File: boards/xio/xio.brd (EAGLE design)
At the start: 170 x 170 mm, 122 parts, among them IC1 AS4C16M16SA-C, IC2 74LVC1G02DBV, IC3 IDTQS3245QSOP20, IC4 IDTQS3245QSOP20, IC5 IDTQS3245QSOP20, IC6 IDTQS3245QSOP20, IC7 IDTQS3245QSOP20, U1 24 MHz Osc. (F535L-24), X1 PCI-E-164SOCKET, X2 PCI-E-164SOCKET, X3 PCI-E-164SOCKET, X4 PCI-E-164SOCKET, X5 PCI-E-164SOCKET, X6 PCI-E-164SOCKET, X7 PCI-E-164SOCKET

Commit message: Start on STM32 power
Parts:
- added C57: 10uF, rcl:C0402K
- added C58: 0.1uF, rcl:C0402K
- added C59, C60: 2.2uF, rcl:C0402K
- added SWD: FTSH-105-01-LM-DV-K, sjg-stm32:SWD_DEBUG
- U$3: value LD49150 -> LD49300
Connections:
- removed net N$4: C31.2, R3.1, U$3.1, U$4.6
- removed net VCCIO: C31.1, R3.2
- new net DBG_RX: SWD.P8, U$22.B4
- new net DBG_TX: SWD.P6, U$22.A7
- new net EN_1V0: R3.1, U$3.1, U$4.1
- new net SWD_CLK: SWD.P4, U$22.A14
- new net SWD_IO: SWD.P2, U$22.A13
- new net VCAP1: C59.1, U$22.L11
- new net VCAP2: C60.1, U$22.E11
- net !RESET!: now also SWD.P10, U$22.J1
- net +3V3: now also C31.1, C57.1, C58.1, R3.2, SWD.P1, U$22.C1, U$22.E10, U$22.E5, U$22.E7, U$22.E8, U$22.E9, U$22.F11, U$22.F4, U$22.F5, U$22.G5, U$22.H11, U$22.H5, U$22.J11, U$22.J5, U$22.K11, U$22.K5, U$22.L10, U$22.L7, U$22.L8, U$22.L9, U$22.P1, U$22.R1, U$4.6
- net GND: now also C31.2, C57.2, C58.2, C59.2, C60.2, SWD.P3, SWD.P5, SWD.P9, U$22.E6, U$22.F10, U$22.F2, U$22.F6, U$22.F7, U$22.F8, U$22.F9, U$22.G10, U$22.G6, U$22.H10, U$22.H6, U$22.J10, U$22.J6, U$22.K10, U$22.K6, U$22.K7, U$22.K8, U$22.K9, U$22.L5, U$22.L6, U$22.M1, U$22.N1

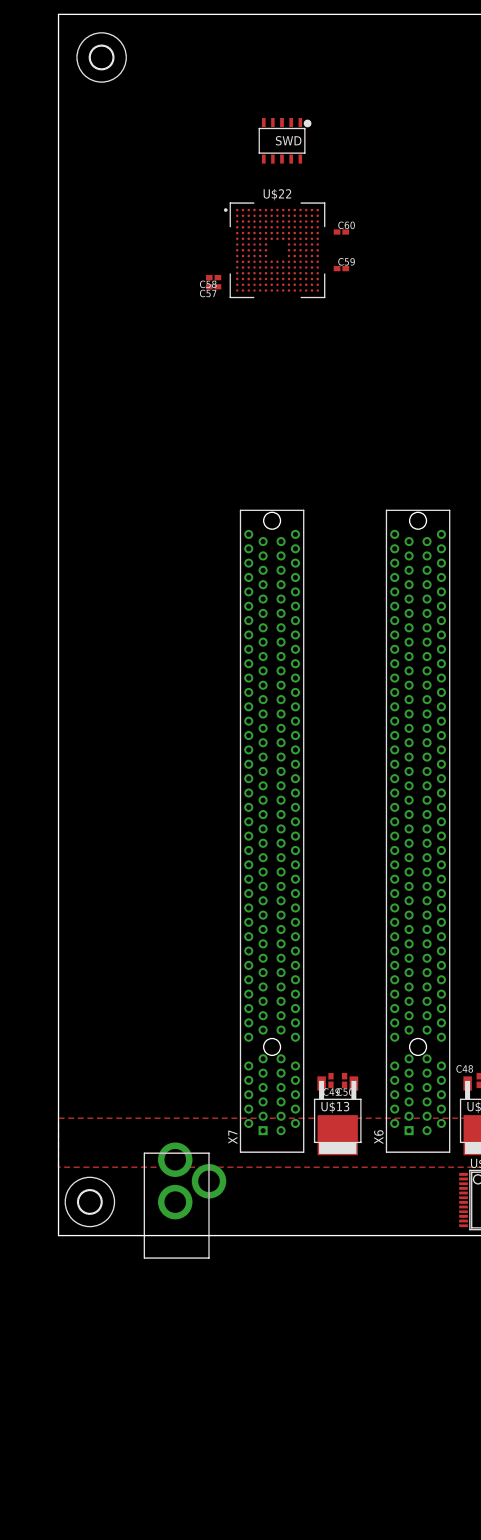
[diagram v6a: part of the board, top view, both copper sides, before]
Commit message: - Implement I2C - Implement SPI - Implement debug leds - Start to implement dual UARTs
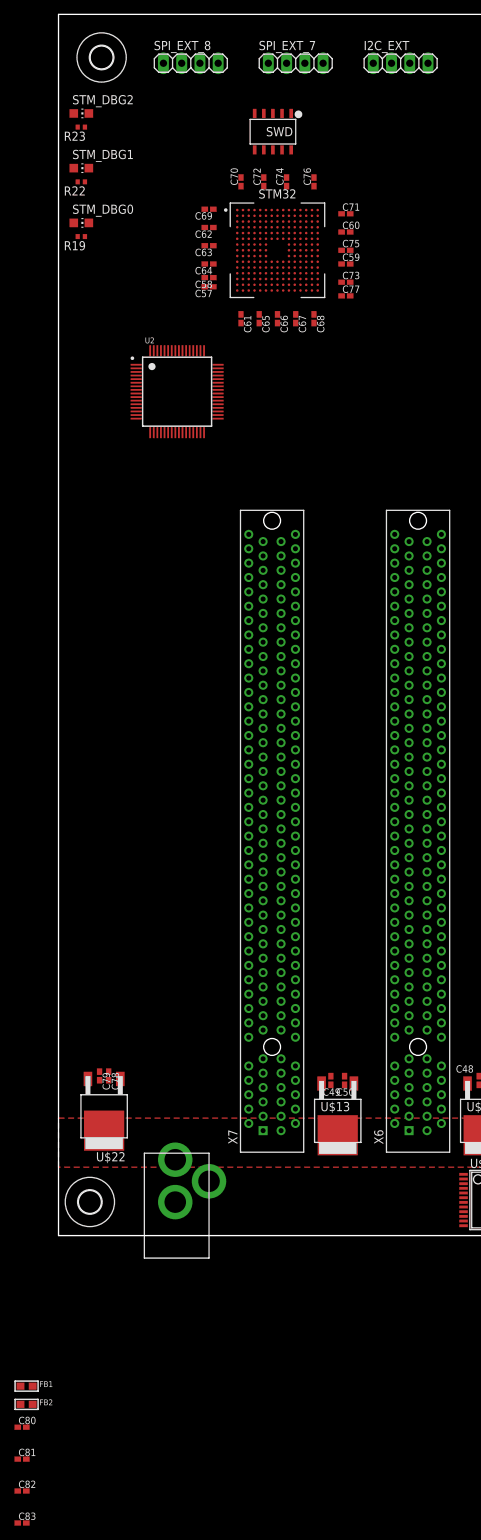
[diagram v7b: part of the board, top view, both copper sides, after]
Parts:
- added C61, C78, C79: 10uF, rcl:C0402K
- added C62, C63, C64, C65, C66, C67, C68, C69, C70, C71, C72, C73, C74, C75, C76, C77, C82, C83: 0.1uF, rcl:C0402K
- added C80, C81: 4.7uF, rcl:C0402K
- added FB1, FB2: 742792651, microbuilder:0603
- added I2C_EXT, SPI_EXT_7, SPI_EXT_8: (no value), pinhead:1X04
- added R19, R22, R23: 1K, rcl:R0402
- added STM32: STM32F777N, sjg-stm32:BGA216C80P15X15_1300X1300X110
- added STM_DBG0, STM_DBG1, STM_DBG2: ok33, led:CHIP-LED0805
- added U2: (no value), microbuilder:LQFP64
- U$22: value STM32F777N -> AP7363-18D-13; device sjg-stm32:BGA216C80P15X15_1300X1300X110 -> sjg-power:TO252-3L
- moved U$22 124.9 mm to (6.35, 14.6), turned to 180 degrees
- moved SWD 1.80 mm to (29.8, 153.7)
- moved C59 0.90 mm to (40.0, 135.3)
- moved C60 0.64 mm to (40.0, 139.7)
- moved C57 0.64 mm to (21.0, 132.1)
- moved C58 0.64 mm to (21.0, 133.3)
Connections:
- new net 1.8V: C79.1, U$22.P$3, U2.12, U2.37, U2.64
- new net I2C_SCL: I2C_EXT.1, I2C_EXT.3, STM32.R13, X1.B44, X2.B44, X3.B44, X4.B44, X5.B44, X6.B44, X7.B44
- new net I2C_SDA: I2C_EXT.2, I2C_EXT.4, STM32.P12, X1.B43, X2.B43, X3.B43, X4.B43, X5.B43, X6.B43, X7.B43
- new net N$17: STM32.K2, STM_DBG0.A
- new net N$20: STM32.K1, STM_DBG1.A
- new net N$21: STM32.A11, STM_DBG2.A
- new net N$22: C81.2, C82.2, FB1.1, U2.4
- new net N$25: R23.1, STM_DBG2.C
- new net N$26: R22.1, STM_DBG1.C
- new net N$27: R19.1, STM_DBG0.C
- new net N$4: C80.1, C83.1, FB2.2, U2.9
- new net PIO_IN0: STM32.R5, X1.B12, X2.B12, X3.B12, X4.B12, X5.B12, X6.B12, X7.B12
- new net PIO_IN1: STM32.R4, X1.B13, X2.B13, X3.B13, X4.B13, X5.B13, X6.B13, X7.B13
- new net PIO_IN2: STM32.M5, X1.B14, X2.B14, X3.B14, X4.B14, X5.B14, X6.B14, X7.B14
- new net PIO_IN3: STM32.A10, X1.B15, X2.B15, X3.B15, X4.B15, X5.B15, X6.B15, X7.B15
- new net PIO_IN4: STM32.A9, X1.B16, X2.B16, X3.B16, X4.B16, X5.B16, X6.B16, X7.B16
- new net PIO_IN5: STM32.A8, X1.B17, X2.B17, X3.B17, X4.B17, X5.B17, X6.B17, X7.B17
- new net PIO_IN6: STM32.B6, X1.B18, X2.B18, X3.B18, X4.B18, X5.B18, X6.B18, X7.B18
- new net PIO_IN7: STM32.B5, X1.B19, X2.B19, X3.B19, X4.B19, X5.B19, X6.B19, X7.B19
- new net PIO_IN_CLK: STM32.M3, X1.B20, X2.B20, X3.B20, X4.B20, X5.B20, X6.B20, X7.B20
- new net PIO_IN_RCV: STM32.H1, X1.B21, X2.B21, X3.B21, X4.B21, X5.B21, X6.B21, X7.B21
- new net PIO_IRQ0: STM32.R2, X1.B22, X2.B22, X3.B22, X4.B22, X5.B22, X6.B22, X7.B22
- new net PIO_IRQ1: STM32.N4, X1.B23, X2.B23, X3.B23, X4.B23, X5.B23, X6.B23, X7.B23
- new net PIO_IRQ2: STM32.P4, X1.B24, X2.B24, X3.B24, X4.B24, X5.B24, X6.B24, X7.B24
- new net PIO_IRQ3: STM32.P3, X1.B25, X2.B25, X3.B25, X4.B25, X5.B25, X6.B25, X7.B25
- new net PIO_IRQ4: STM32.A2, X1.B26, X2.B26, X3.B26, X4.B26, X5.B26, X6.B26, X7.B26
- new net PIO_IRQ5: STM32.A1, X1.B27, X2.B27, X3.B27, X4.B27, X5.B27, X6.B27, X7.B27
- new net PIO_IRQ6: STM32.B1, X1.B28, X2.B28, X3.B28, X4.B28, X5.B28, X6.B28, X7.B28
- new net PIO_IRQ7: STM32.B2, X1.B29, X2.B29, X3.B29, X4.B29, X5.B29, X6.B29, X7.B29
- new net PIO_OUT0: STM32.E14, X1.B30, X2.B30, X3.B30, X4.B30, X5.B30, X6.B30, X7.B30
- new net PIO_OUT1: STM32.D14, X1.B31, X2.B31, X3.B31, X4.B31, X5.B31, X6.B31, X7.B31
- new net PIO_OUT2: STM32.C14, X1.B32, X2.B32, X3.B32, X4.B32, X5.B32, X6.B32, X7.B32
- new net PIO_OUT3: STM32.C13, X1.B33, X2.B33, X3.B33, X4.B33, X5.B33, X6.B33, X7.B33
- new net PIO_OUT4: STM32.C3, X1.B34, X2.B34, X3.B34, X4.B34, X5.B34, X6.B34, X7.B34
- new net PIO_OUT5: STM32.D3, X1.B35, X2.B35, X3.B35, X4.B35, X5.B35, X6.B35, X7.B35
- new net PIO_OUT6: STM32.D6, X1.B36, X2.B36, X3.B36, X4.B36, X5.B36, X6.B36, X7.B36
- new net PIO_OUT7: STM32.D4, X1.B37, X2.B37, X3.B37, X4.B37, X5.B37, X6.B37, X7.B37
- new net PIO_OUT_CLK: STM32.M12, X1.B38, X2.B38, X3.B38, X4.B38, X5.B38, X6.B38, X7.B38
- new net PIO_OUT_RCV: STM32.H4, X1.B39, X2.B39, X3.B39, X4.B39, X5.B39, X6.B39, X7.B39
- new net PIO_SEL0: STM32.N10, X1.B40, X2.B40, X3.B40, X4.B40, X5.B40, X6.B40, X7.B40
- new net PIO_SEL1: STM32.M10, X1.B41, X2.B41, X3.B41, X4.B41, X5.B41, X6.B41, X7.B41
- new net PIO_SEL2: STM32.M11, X1.B42, X2.B42, X3.B42, X4.B42, X5.B42, X6.B42, X7.B42
- new net SPI_CLK: SPI_EXT_7.1, SPI_EXT_8.1, STM32.K14, X1.B45, X2.B45, X3.B45, X4.B45, X5.B45, X6.B45, X7.B45
- new net SPI_MISO: SPI_EXT_7.2, SPI_EXT_8.2, STM32.R14, X1.B46, X2.B46, X3.B46, X4.B46, X5.B46, X6.B46, X7.B46
- new net SPI_MOSI: SPI_EXT_7.3, SPI_EXT_8.3, STM32.R15, X1.B47, X2.B47, X3.B47, X4.B47, X5.B47, X6.B47, X7.B47
- new net SPI_SS0: STM32.J15, X1.B48
- new net SPI_SS1: STM32.J14, X2.B48
- new net SPI_SS2: STM32.D9, X3.B48
- new net SPI_SS3: STM32.C8, X4.B48
- new net SPI_SS4: STM32.C2, X5.B48
- new net SPI_SS5: STM32.E4, X6.B48
- new net SPI_SS6: STM32.F3, X7.B48
- new net SPI_SS7: SPI_EXT_7.4, STM32.N3
- new net SPI_SS8: SPI_EXT_8.4, STM32.A13
- net !RESET!: now also STM32.J1; no longer U$22.J1
- net +3V3: now also C61.1, C62.1, C63.1, C64.1, C65.1, C66.1, C67.1, C68.1, C69.1, C70.1, C71.1, C72.1, C73.1, C74.1, C75.1, C76.1, C77.1, FB1.2, FB2.1, STM32.C1, STM32.E10, STM32.E5, STM32.E7, STM32.E8, STM32.E9, STM32.F11, STM32.F4, STM32.F5, STM32.G5, STM32.H11, STM32.H5, STM32.J11, STM32.J5, STM32.K11, STM32.K5, STM32.L10, STM32.L7, STM32.L8, STM32.L9, STM32.P1, STM32.R1, U2.20, U2.31, U2.42, U2.56; no longer U$22.C1, U$22.E10, U$22.E5, U$22.E7, U$22.E8, U$22.E9, U$22.F11, U$22.F4, U$22.F5, U$22.G5, U$22.H11, U$22.H5, U$22.J11, U$22.J5, U$22.K11, U$22.K5, U$22.L10, U$22.L7, U$22.L8, U$22.L9, U$22.P1, U$22.R1
- net +5V: now also C78.1, U$22.P$1
- net DBG_RX: now also STM32.B4; no longer U$22.B4
- net DBG_TX: now also STM32.A7; no longer U$22.A7
- net GND: now also C61.2, C62.2, C63.2, C64.2, C65.2, C66.2, C67.2, C68.2, C69.2, C70.2, C71.2, C72.2, C73.2, C74.2, C75.2, C76.2, C77.2, C78.2, C79.2, C80.2, C81.1, C82.1, C83.2, R19.2, R22.2, R23.2, STM32.E6, STM32.F10, STM32.F2, STM32.F6, STM32.F7, STM32.F8, STM32.F9, STM32.G10, STM32.G6, STM32.H10, STM32.H6, STM32.J10, STM32.J6, STM32.K10, STM32.K6, STM32.K7, STM32.K8, STM32.K9, STM32.L5, STM32.L6, STM32.M1, STM32.N1, U$22.P$2, U2.1, U2.10, U2.11, U2.13, U2.15, U2.25, U2.35, U2.47, U2.5, U2.51; no longer U$22.E6, U$22.F10, U$22.F2, U$22.F6, U$22.F7, U$22.F8, U$22.F9, U$22.G10, U$22.G6, U$22.H10, U$22.H6, U$22.J10, U$22.J6, U$22.K10, U$22.K6, U$22.K7, U$22.K8, U$22.K9, U$22.L5, U$22.L6, U$22.M1, U$22.N1
- net SWD_CLK: now also STM32.A14; no longer U$22.A14
- net SWD_IO: now also STM32.A15; no longer U$22.A13
- net VCAP1: now also STM32.L11; no longer U$22.L11
- net VCAP2: now also STM32.E11; no longer U$22.E11
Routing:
- added copper zone on layer 15, net +3V3
- added copper zone on layer 2, net GND

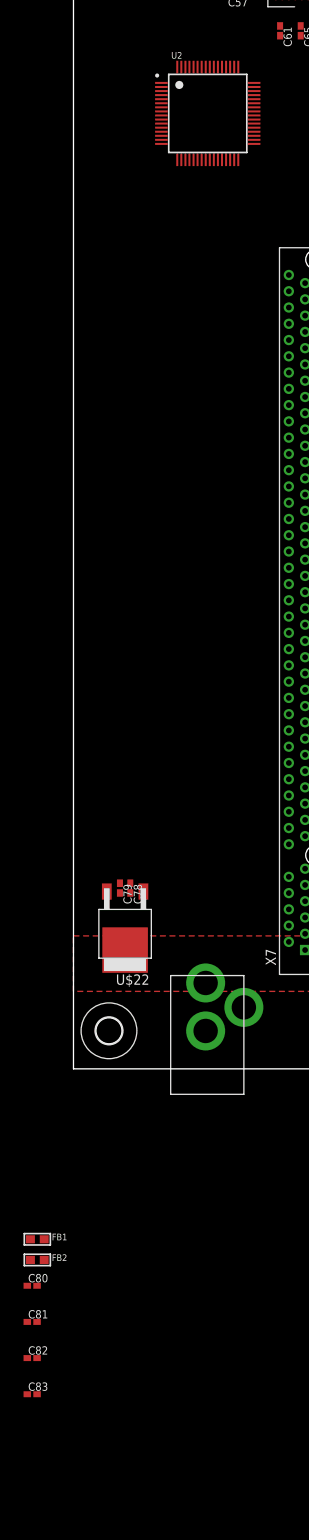
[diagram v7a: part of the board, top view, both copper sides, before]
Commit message: Start to create the quad interface schematic
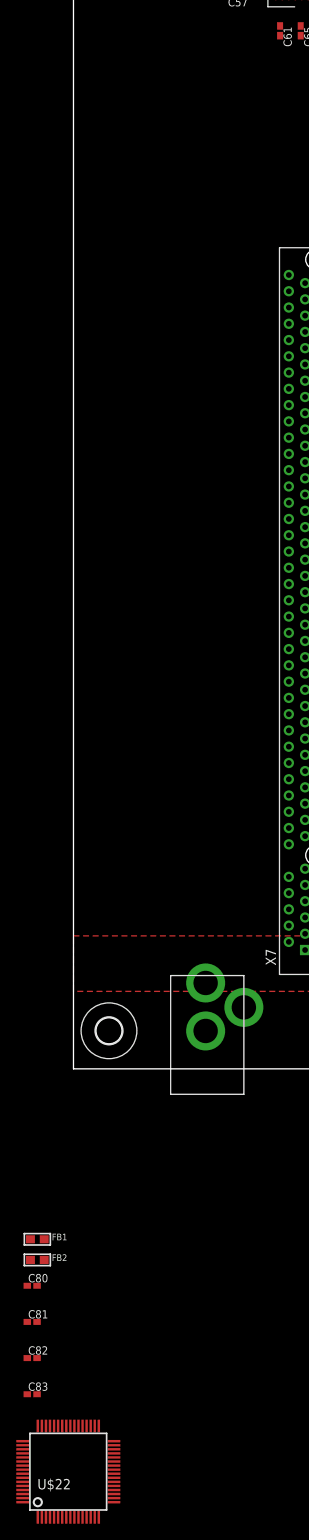
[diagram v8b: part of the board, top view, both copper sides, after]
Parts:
- removed C78, C79: 10uF, rcl:C0402K
- removed U2: (no value), microbuilder:LQFP64
- U$22: value AP7363-18D-13 -> FT4232H; device sjg-power:TO252-3L -> sjg-ftdi:SQFP-S-10X10-64
- moved U$22 64.5 mm to (-0.64, -49.5), turned to 0 degrees
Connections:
- removed net 1.8V: C79.1, U$22.P$3, U2.12, U2.37, U2.64
- net +3V3: no longer U2.20, U2.31, U2.42, U2.56
- net +5V: no longer C78.1, U$22.P$1
- net GND: no longer C78.2, C79.2, U$22.P$2, U2.1, U2.10, U2.11, U2.13, U2.15, U2.25, U2.35, U2.47, U2.5, U2.51
- net N$22: no longer U2.4
- net N$4: no longer U2.9
